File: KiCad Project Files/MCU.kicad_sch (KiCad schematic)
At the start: 24 parts, among them SW1 Reset, U1 RP2040, U2 W25Q128JVS, Y1 12MHz

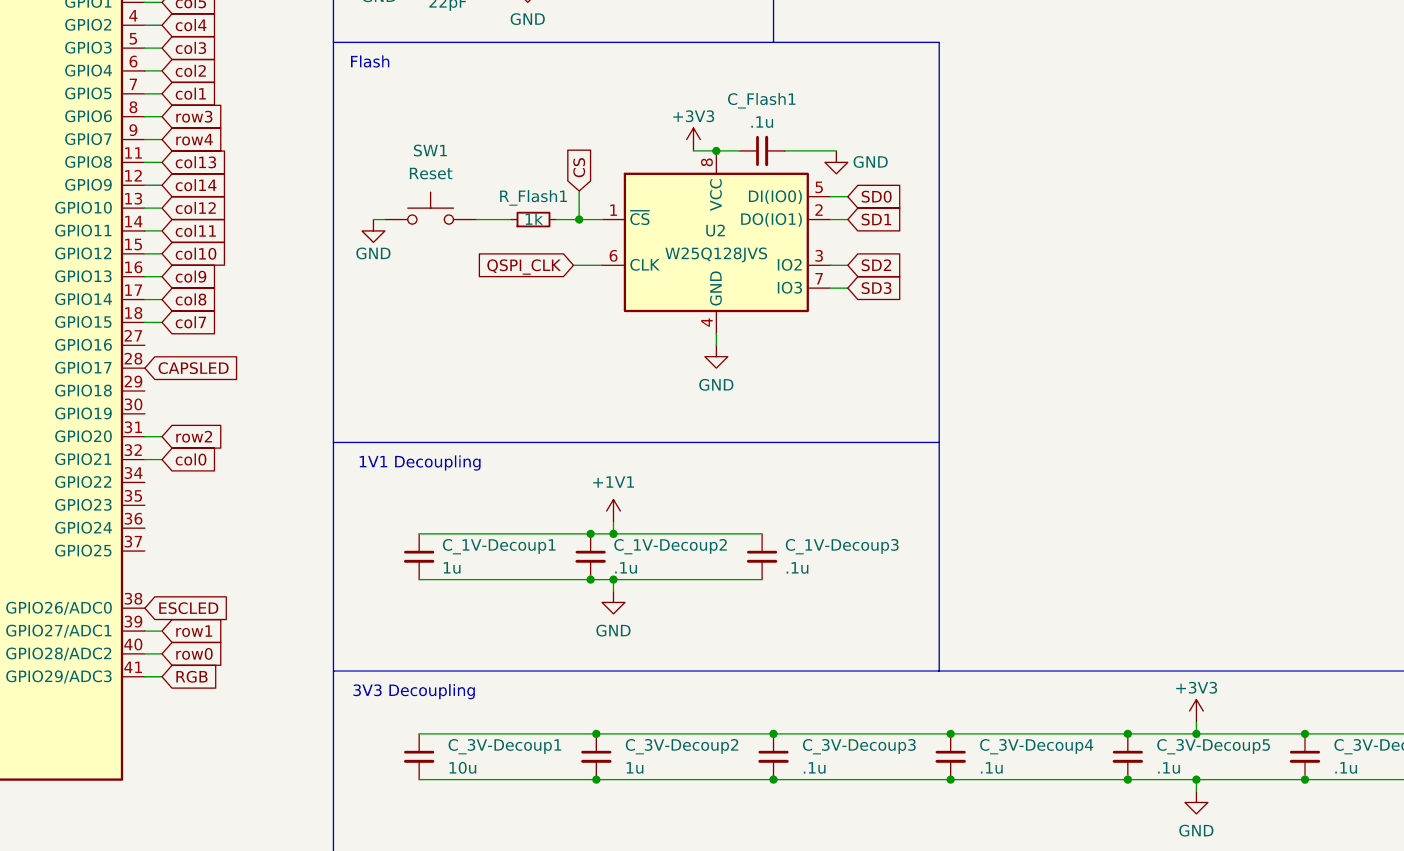
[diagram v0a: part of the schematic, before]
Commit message: QoL Improvements
- Add physical button for Bootloader and Reset.
- Add logic level shifter for the leds according to suggestion by Sleepdealer.
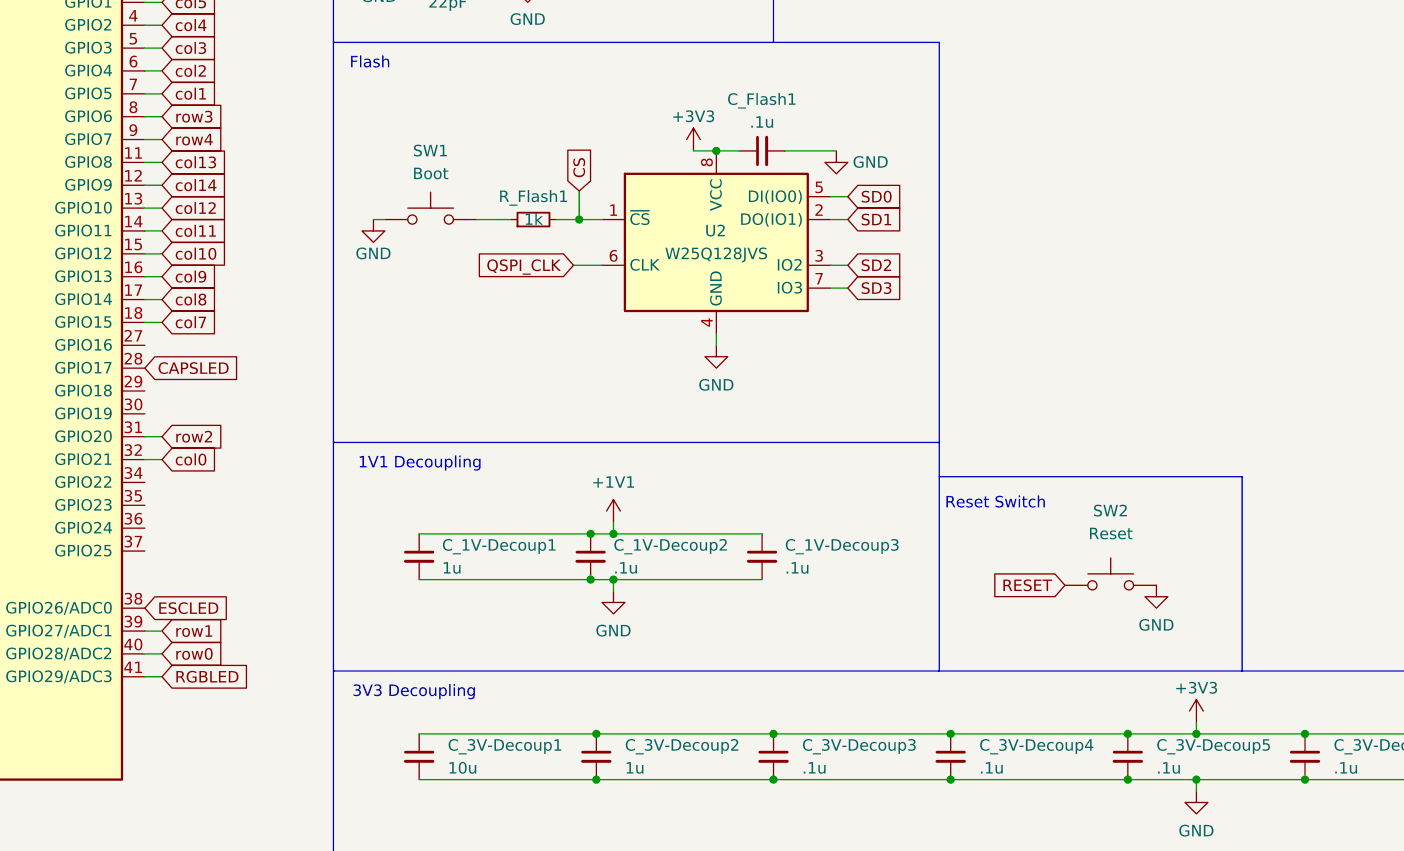
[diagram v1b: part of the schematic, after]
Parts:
- added SW2: Reset, Button_Switch_SMD:SW_SPST_TL3342, symbol Switch:SW_Push
- SW1: value Reset -> Boot; footprint Connector_PinHeader_1.27mm:PinHeader_1x02_P1.27mm_Vertical -> Button_Switch_SMD:SW_SPST_TL3342
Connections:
- net GND: now also SW2.2
- net RESET: now also SW2.1
- net RGB renamed RGBLED
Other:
- note added: "Reset Switch"
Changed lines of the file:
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@@
+    (stroke (width 0) (type default) (color 0 0 0 0))
+  )
+  (polyline (pts (xy 163.195 86.36) (xy 196.85 86.36))
     (stroke (width 0) (type default) (color 0 0 0 0))
   )
@@
     (stroke (width 0) (type default) (color 0 0 0 0))
   )
+  (polyline (pts (xy 196.85 86.36) (xy 196.85 107.95))
+    (stroke (width 0) (type default) (color 0 0 0 0))
+  )
   (polyline (pts (xy 95.885 12.7) (xy 95.885 133.35))
     (stroke (width 0) (type default) (color 0 0 0 0))
@@
   (polyline (pts (xy 95.885 107.95) (xy 163.195 107.95))
     (stroke (width 0) (type default) (color 0 0 0 0))
+  )
+  (text "Reset Switch" (at 163.83 90.17 0)
+    (effects (font (size 1.27 1.27)) (justify left bottom))
   )
   (text "Flash\n" (at 102.235 41.275 180)
@@
     )
   )
+  (global_label "RESET" (shape input) (at 177.165 98.425 180) (fields_autoplaced)
+    (effects (font (size 1.27 1.27)) (justify right))
+    (property "Intersheet References" "${INTERSHEET_REFS}" (id 0) (at 169.0067 98.3456 0)
+      (effects (font (size 1.27 1.27)) (justify right) hide)
+    )
+  )
   (global_label "col3" (shape input) (at 76.835 38.735 0) (fields_autoplaced)
     (effects (font (size 1.27 1.27)) (justify left))
@@
     )
   )
-  (global_label "RGB" (shape input) (at 76.835 108.585 0) (fields_autoplaced)
-    (effects (font (size 1.27 1.27)) (justify left))
-    (property "Intersheet References" "${INTERSHEET_REFS}" (id 0) (at 83.0581 108.5056 0)
+  (global_label "RGBLED" (shape input) (at 76.835 108.585 0) (fields_autoplaced)
+    (effects (font (size 1.27 1.27)) (justify left))
+    (property "Intersheet References" "${INTERSHEET_REFS}" (id 0) (at 86.5052 108.5056 0)
       (effects (font (size 1.27 1.27)) (justify left) hide)
     )
@@
     (pin "1")
     (pin "2")
+  )
+  (symbol (lib_id "power:GND") (at 187.325 98.425 0) (unit 1)
+    (in_bom yes) (on_board yes) (fields_autoplaced)
+    (property "Reference" "#PWR0146" (id 0) (at 187.325 104.775 0)
+      (effects (font (size 1.27 1.27)) hide)
+    )
+    (property "Value" "GND" (id 1) (at 187.325 102.87 0))
+    (property "Footprint" "" (id 2) (at 187.325 98.425 0)
+      (effects (font (size 1.27 1.27)) hide)
+    )
+    (property "Datasheet" "" (id 3) (at 187.325 98.425 0)
+      (effects (font (size 1.27 1.27)) hide)
+    )
+    (pin "1")
   )
   (symbol (lib_id "power:GND") (at 191.77 121.285 0) (unit 1)
@@
     (pin "1")
   )
+  (symbol (lib_id "Switch:SW_Push") (at 182.245 98.425 0) (unit 1)
+    (in_bom yes) (on_board yes) (fields_autoplaced)
+    (property "Reference" "SW2" (id 0) (at 182.245 90.17 0))
+    (property "Value" "Reset" (id 1) (at 182.245 92.71 0))
+    (property "Footprint" "Button_Switch_SMD:SW_SPST_TL3342" (id 2) (at 182.245 93.345 0)
+      (effects (font (size 1.27 1.27)) hide)
+    )
+    (property "Datasheet" "~" (id 3) (at 182.245 93.345 0)
+      (effects (font (size 1.27 1.27)) hide)
+    )
+    (pin "1")
+    (pin "2")
+  )
   (symbol (lib_id "power:+3V3") (at 31.75 76.835 0) (unit 1)
     (in_bom yes) (on_board yes)
@@
     (in_bom yes) (on_board yes) (fields_autoplaced)
     (property "Reference" "SW1" (id 0) (at 106.68 50.165 0))
-    (property "Value" "Reset" (id 1) (at 106.68 52.705 0))
-    (property "Footprint" "Connector_PinHeader_1.27mm:PinHeader_1x02_P1.27mm_Vertical" (id 2) (at 106.68 52.705 0)
-      (effects (font (size 1.27 1.27)) hide)
-    )
+    (property "Value" "Boot" (id 1) (at 106.68 52.705 0))
+    (property "Footprint" "Button_Switch_SMD:SW_SPST_TL3342" (id 2) (at 106.68 52.705 0)
+      (effects (font (size 1.27 1.27)) hide)
+    )
